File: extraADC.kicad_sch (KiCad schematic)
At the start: 16 parts, among them J10 Conn_02x08_Odd_Even, Q14 DMP2160UWQ-7, U42 ADS1015BQDGSRQ1, U43 ADS1015BQDGSRQ1

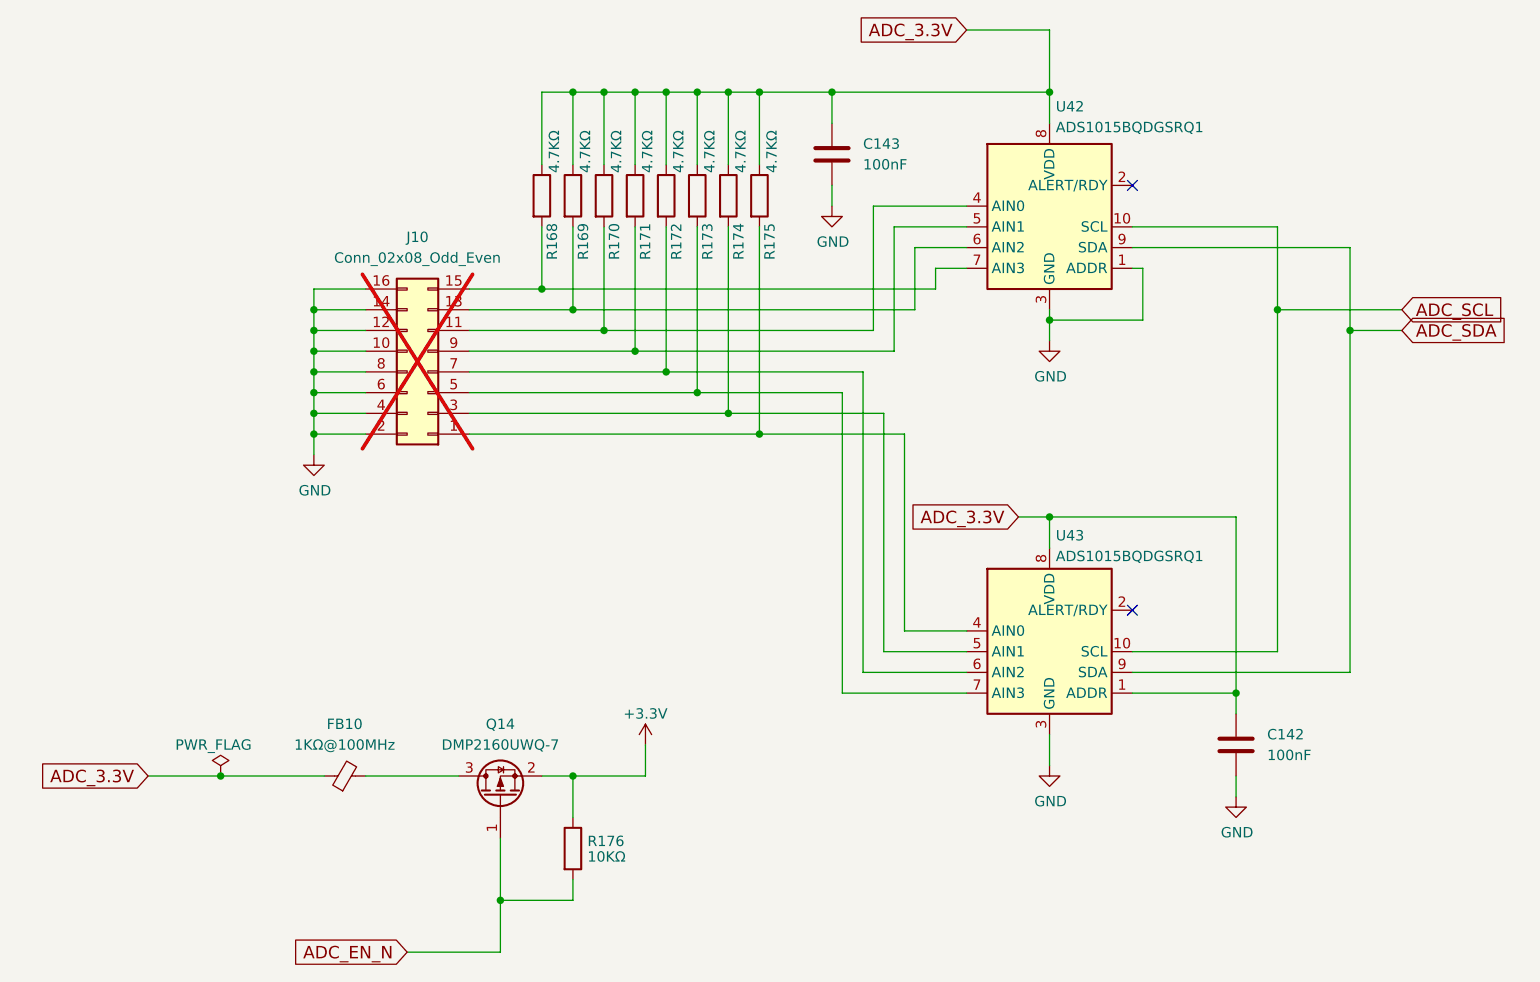
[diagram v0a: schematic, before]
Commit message: Rework the ADC connector
Figured out a way to put a real connector on there.

Signed-off-by: Corey Minyard <corey@minyard.net>
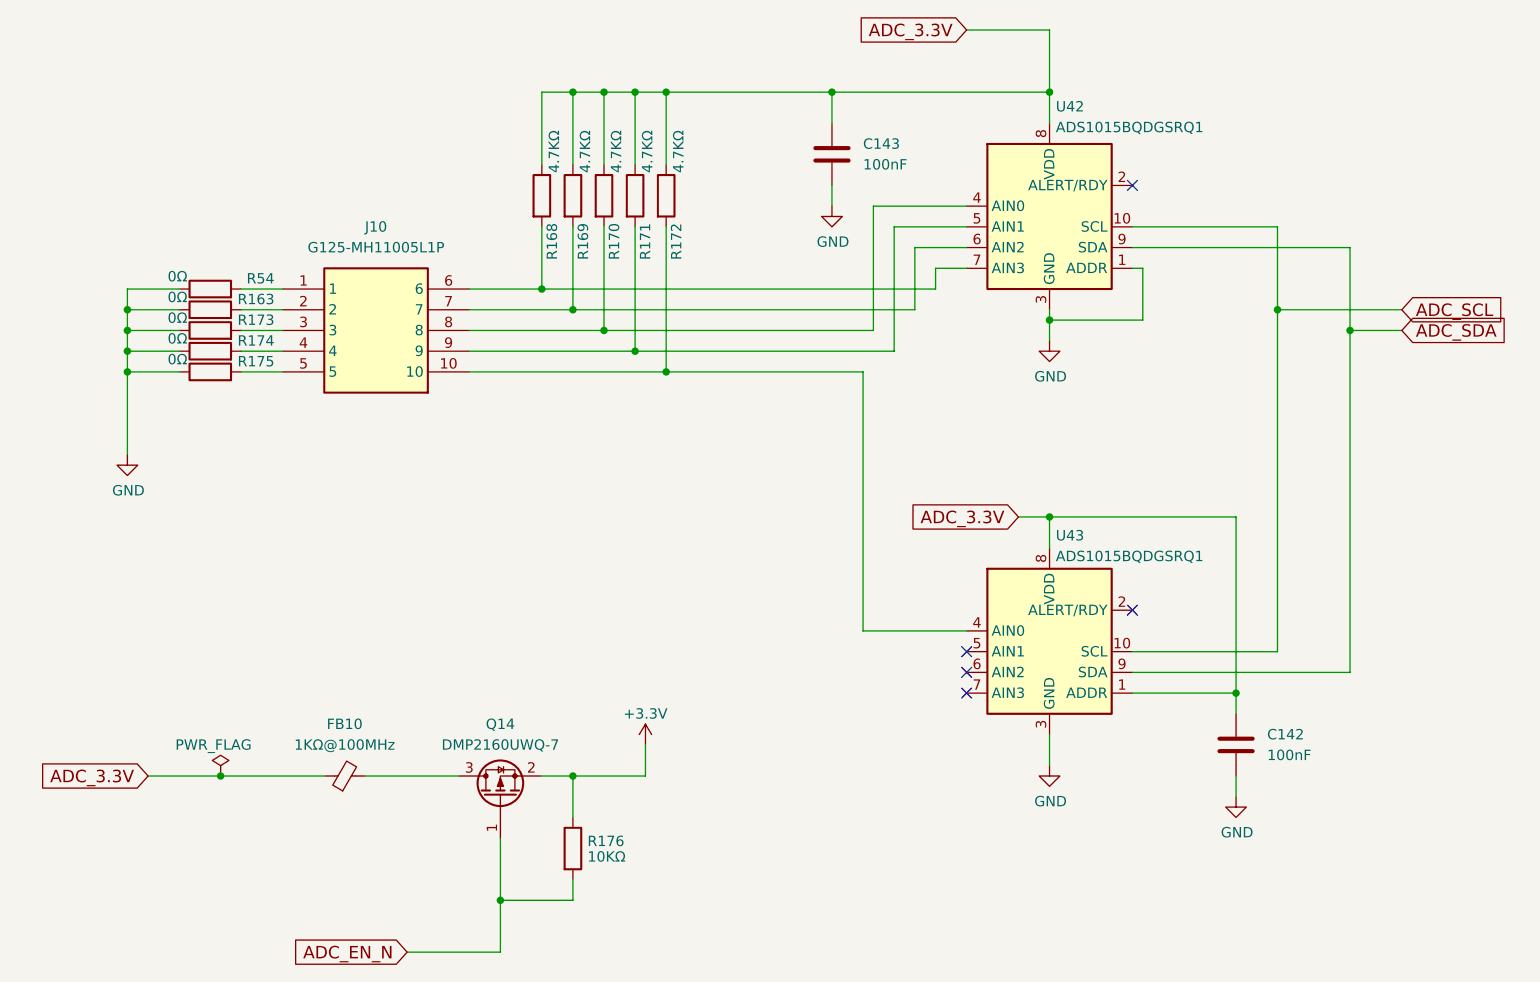
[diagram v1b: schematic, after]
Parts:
- removed J10: Conn_02x08_Odd_Even, Connector_PinHeader_1.27mm:PinHeader_2x08_P1.27mm_Vertical, symbol Connector_Generic:Conn_02x08_Odd_Even
- added J10: G125-MH11005L1P, PacSatDev_misc:G125-MH11005L1P, symbol PACSAT_DEV_misc:G125-MH11005L1P
- added R163, R54: 0Ω, Resistor_SMD:R_0402_1005Metric_Pad0.72x0.64mm_HandSolder, symbol Device:R
- R173, R174, R175: value 4.7KΩ -> 0Ω
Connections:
- net ADC_3.3V: no longer R173.1, R174.1, R175.1
- net GND: now also R173.1, R174.1, R175.1, R163.1, R54.1
- net at R173.2: now also J10.3; no longer U43.7 (AIN3)
- net at R171.2, U42.5 (AIN1): now also J10.9
- net at R174.2: now also J10.4; no longer U43.5 (AIN1)
- net at R169.2, U42.6 (AIN2): now also J10.7
- net at R175.2: now also J10.5; no longer U43.4 (AIN0)
- net at R172.2: now also U43.4 (AIN0), J10.10; no longer U43.6 (AIN2)
- net at R168.2, U42.7 (AIN3): now also J10.6
- net at R170.2, U42.4 (AIN0): now also J10.8
- new net: J10.2, R163.2
- new net: J10.1, R54.2
- no-connect marks 2 -> 5

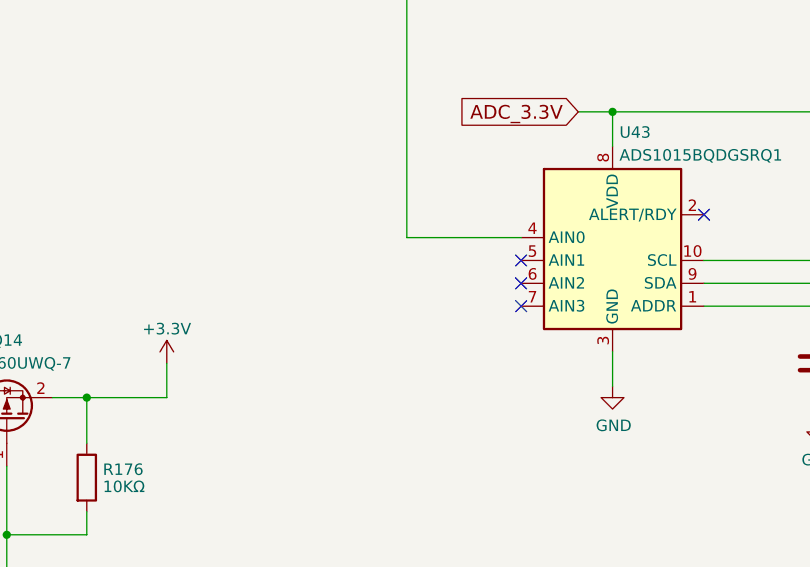
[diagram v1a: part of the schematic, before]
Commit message: Add some DNS 0-ohm resistors to the unused extra ADC outputs
To make it easier to use them later.

Signed-off-by: Corey Minyard <corey@minyard.net>
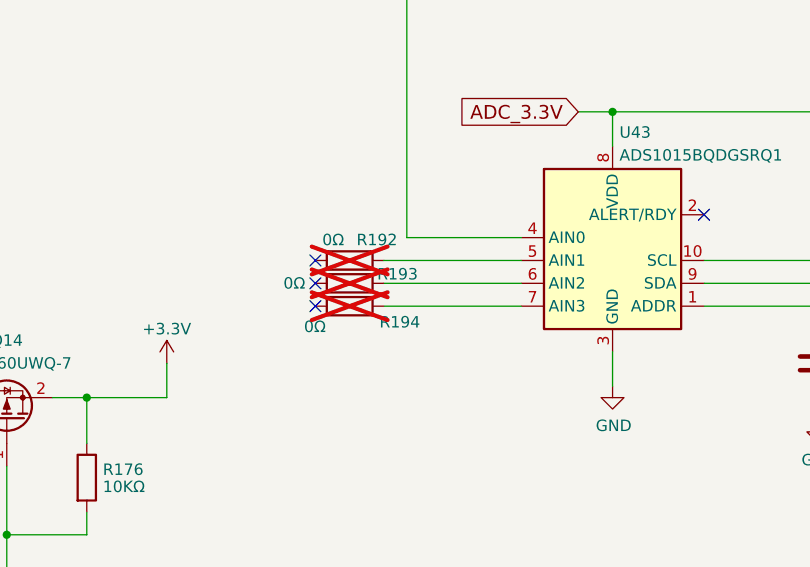
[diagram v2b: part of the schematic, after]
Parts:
- added R192, R193, R194: 0Ω, Resistor_SMD:R_0402_1005Metric_Pad0.72x0.64mm_HandSolder, symbol Device:R
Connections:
- net at U43.5 (AIN1): now also R192.1
- net at U43.6 (AIN2): now also R193.1
- net at U43.7 (AIN3): now also R194.1
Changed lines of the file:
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@@
 	)
 	(no_connect
-		(at 149.86 139.7)
+		(at 127 137.16)
 	)
 	(no_connect
-		(at 149.86 134.62)
+		(at 127 134.62)
+	)
+	(no_connect
+		(at 127 139.7)
 	)
 	(no_connect
@@
 		(at 170.18 77.47)
 	)
-	(no_connect
-		(at 149.86 137.16)
-	)
 	(wire
 		(pts
@@
 	(wire
 		(pts
+			(xy 134.62 134.62) (xy 149.86 134.62)
+		)
+		(stroke
+			(width 0)
+			(type default)
+		)
+	)
+	(wire
+		(pts
 			(xy 101.6 66.04) (xy 105.41 66.04)
 		)
@@
 	(wire
 		(pts
+			(xy 134.62 139.7) (xy 149.86 139.7)
+		)
+		(stroke
+			(width 0)
+			(type default)
+		)
+	)
+	(wire
+		(pts
 			(xy 92.71 171.45) (xy 92.71 165.1)
 		)
@@
 		(pts
 			(xy 46.99 100.33) (xy 46.99 110.49)
+		)
+		(stroke
+			(width 0)
+			(type default)
+		)
+	)
+	(wire
+		(pts
+			(xy 134.62 137.16) (xy 149.86 137.16)
 		)
 		(stroke
@@
 	(symbol
 		(lib_id "Device:R")
+		(at 130.81 139.7 270)
+		(unit 1)
+		(exclude_from_sim no)
+		(in_bom no)
+		(on_board yes)
+		(dnp yes)
+		(property "Reference" "R194"
+			(at 134.112 141.478 90)
+			(effects
+				(font
+					(size 1.27 1.27)
+				)
+				(justify left)
+			)
+		)
+		(property "Value" "0Ω"
+			(at 125.73 141.986 90)
+			(effects
+				(font
+					(size 1.27 1.27)
+				)
+				(justify left)
+			)
+		)
+		(property "Footprint" "Resistor_SMD:R_0402_1005Metric_Pad0.72x0.64mm_HandSolder"
+			(at 130.81 137.922 90)
+			(effects
+				(font
+					(size 1.27 1.27)
+				)
+				(hide yes)
+			)
+		)
+		(property "Datasheet" "~"
+			(at 130.81 139.7 0)
+			(effects
+				(font
+					(size 1.27 1.27)
+				)
+				(hide yes)
+			)
+		)
+		(property "Description" ""
+			(at 130.81 139.7 0)
+			(effects
+				(font
+					(size 1.27 1.27)
+				)
+			)
+		)
+		(pin "1"
+		)
+		(pin "2"
+		)
+		(instances
+			(project "PacSat_AFSK"
+				(path "/cc9f42d2-6985-41ac-acab-5ab7b01c5b38/75b01062-9747-4556-85bc-485f2c3c99d3/0c35b1f3-051c-4645-bbee-ec3d7e916024"
+					(reference "R194")
+					(unit 1)
+				)
+			)
+		)
+	)
+	(symbol
+		(lib_id "Device:R")
 		(at 57.15 92.71 90)
 		(unit 1)
@@
 				(path "/cc9f42d2-6985-41ac-acab-5ab7b01c5b38/75b01062-9747-4556-85bc-485f2c3c99d3/0c35b1f3-051c-4645-bbee-ec3d7e916024"
 					(reference "R175")
+					(unit 1)
+				)
+			)
+		)
+	)
+	(symbol
+		(lib_id "Device:R")
+		(at 130.81 134.62 270)
+		(unit 1)
+		(exclude_from_sim no)
+		(in_bom no)
+		(on_board yes)
+		(dnp yes)
+		(property "Reference" "R192"
+			(at 131.572 132.334 90)
+			(effects
+				(font
+					(size 1.27 1.27)
+				)
+				(justify left)
+			)
+		)
+		(property "Value" "0Ω"
+			(at 127.762 132.334 90)
+			(effects
+				(font
+					(size 1.27 1.27)
+				)
+				(justify left)
+			)
+		)
+		(property "Footprint" "Resistor_SMD:R_0402_1005Metric_Pad0.72x0.64mm_HandSolder"
+			(at 130.81 132.842 90)
+			(effects
+				(font
+					(size 1.27 1.27)
+				)
+				(hide yes)
+			)
+		)
+		(property "Datasheet" "~"
+			(at 130.81 134.62 0)
+			(effects
+				(font
+					(size 1.27 1.27)
+				)
+				(hide yes)
+			)
+		)
+		(property "Description" ""
+			(at 130.81 134.62 0)
+			(effects
+				(font
+					(size 1.27 1.27)
+				)
+			)
+		)
+		(pin "1"
+		)
+		(pin "2"
+		)
+		(instances
+			(project "PacSat_AFSK"
+				(path "/cc9f42d2-6985-41ac-acab-5ab7b01c5b38/75b01062-9747-4556-85bc-485f2c3c99d3/0c35b1f3-051c-4645-bbee-ec3d7e916024"
+					(reference "R192")
 					(unit 1)
 				)
@@
 					(unit 1)
 				)
+			)
+		)
+	)
+	(symbol
+		(lib_id "Device:R")
+		(at 130.81 137.16 270)
+		(unit 1)
+		(exclude_from_sim no)
+		(in_bom no)
+		(on_board yes)
+		(dnp yes)
+		(property "Reference" "R193"
+			(at 133.858 136.144 90)
+			(effects
+				(font
+					(size 1.27 1.27)
+				)
+				(justify left)
+			)
+		)
+		(property "Value" "0Ω"
+			(at 123.444 137.16 90)
+			(effects
+				(font
+					(size 1.27 1.27)
+				)
+				(justify left)
+			)
+		)
+		(property "Footprint" "Resistor_SMD:R_0402_1005Metric_Pad0.72x0.64mm_HandSolder"
+			(at 130.81 135.382 90)
+			(effects
+				(font
+					(size 1.27 1.27)
+				)
+				(hide yes)
+			)
+		)
+		(property "Datasheet" "~"
+			(at 130.81 137.16 0)
+			(effects
+				(font
+					(size 1.27 1.27)
+				)
+				(hide yes)
+			)
+		)
+		(property "Description" ""
+			(at 130.81 137.16 0)
+			(effects
+				(font
+					(size 1.27 1.27)
+				)
+			)
+		)
+		(pin "1"
+		)
+		(pin "2"
+		)
+		(instances
+			(project "PacSat_AFSK"
+				(path "/cc9f42d2-6985-41ac-acab-5ab7b01c5b38/75b01062-9747-4556-85bc-485f2c3c99d3/0c35b1f3-051c-4645-bbee-ec3d7e916024"
+					(reference "R193")
+					(unit 1)
+				)
